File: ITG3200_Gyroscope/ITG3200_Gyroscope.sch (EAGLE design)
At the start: 11 parts, among them U1 ITG-3200

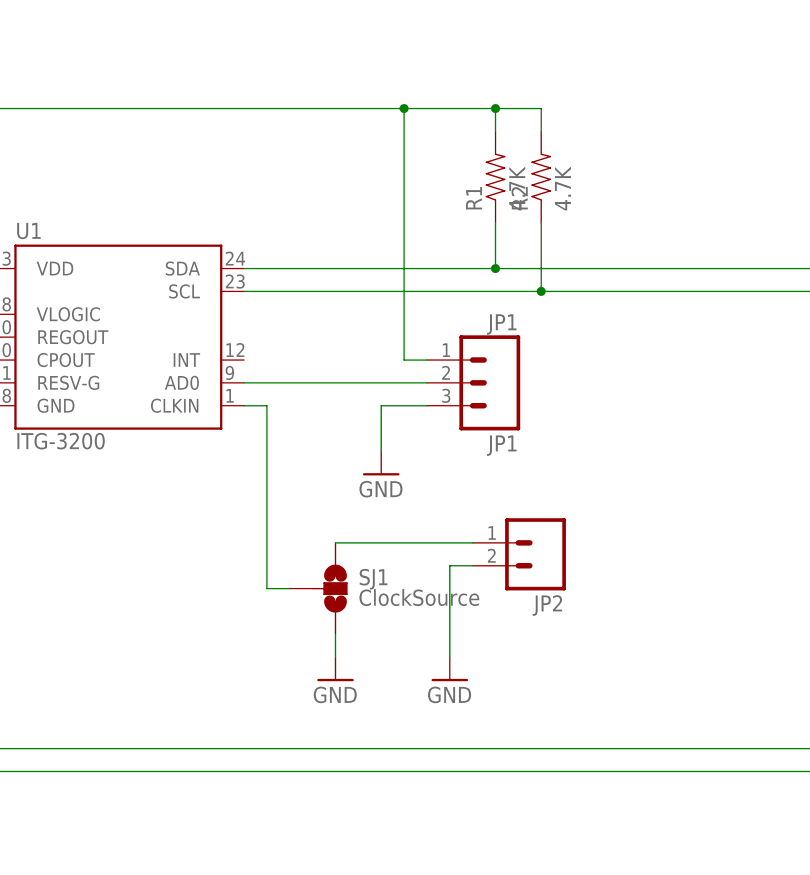
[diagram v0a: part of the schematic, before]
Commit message: Added OLED Shield Added LiPo Battery Charger Shield Updated outlines of all shields to match the cutout of the nodemcu board
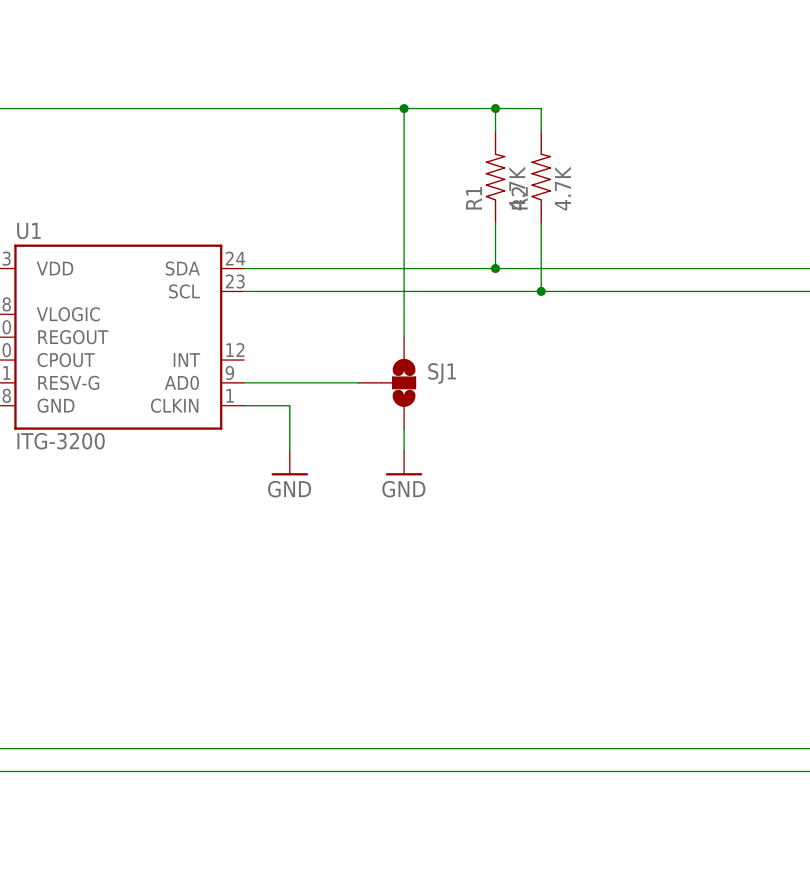
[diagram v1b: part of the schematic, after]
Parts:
- removed JP1: JP1, SparkFun:M03PTH
- removed JP2: (no value), SparkFun:M02LOCK
- SJ1: value ClockSource -> (none); device SparkFun:SOLDERJUMPER_2WAYPASTE2&3 -> SparkFun:SOLDERJUMPER_2WAYT
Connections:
- removed net N$10: JP2.1, SJ1.1
- removed net N$11: SJ1.2, U1.CLKIN
- net +3V3: now also SJ1.1; no longer JP1.1
- net GND: now also U1.CLKIN; no longer JP1.3, JP2.2
- net N$1: now also SJ1.2; no longer JP1.2
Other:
- moved on the sheet: SJ1
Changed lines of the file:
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@@
 <?xml version="1.0" encoding="utf-8"?>
 <!DOCTYPE eagle SYSTEM "eagle.dtd">
-<eagle version="7.3.0">
+<eagle version="7.4.0">
 <drawing>
 <settings>
@@
 <part name="R2" library="SparkFun" deviceset="RESISTOR" device="0402-RES" value="4.7K"/>
 <part name="+3V2" library="supply1" deviceset="+3V3" device=""/>
-<part name="JP1" library="SparkFun" deviceset="M03" device="PTH" value="JP1"/>
 <part name="GND7" library="SparkFun" deviceset="GND" device=""/>
 <part name="U1" library="SparkFun" deviceset="ITG-3200" device=""/>
@@
 <part name="GND10" library="SparkFun" deviceset="GND" device=""/>
 <part name="GND11" library="SparkFun" deviceset="GND" device=""/>
-<part name="JP2" library="SparkFun" deviceset="M02" device="LOCK"/>
 <part name="GND12" library="SparkFun" deviceset="GND" device=""/>
-<part name="SJ1" library="SparkFun" deviceset="SOLDERJUMPER_2WAY" device="PASTE2&amp;3" value="ClockSource"/>
-<part name="GND13" library="SparkFun" deviceset="GND" device=""/>
 <part name="U$2" library="NerduinoShieldLib" deviceset="NERDSHIELD" device=""/>
 <part name="+3V4" library="supply1" deviceset="+3V3" device=""/>
+<part name="SJ1" library="SparkFun" deviceset="SOLDERJUMPER_2WAY" device="T"/>
 </parts>
 <sheets>
@@
 <instance part="R2" gate="G$1" x="177.8" y="114.3" rot="R90"/>
 <instance part="+3V2" gate="G$1" x="96.52" y="129.54"/>
-<instance part="JP1" gate="G$1" x="172.72" y="91.44" rot="R180"/>
-<instance part="GND7" gate="1" x="160.02" y="81.28"/>
+<instance part="GND7" gate="1" x="162.56" y="81.28"/>
 <instance part="U1" gate="G$1" x="129.54" y="96.52"/>
 <instance part="GND8" gate="1" x="114.3" y="83.82"/>
@@
 <instance part="GND10" gate="1" x="93.98" y="78.74"/>
 <instance part="GND11" gate="1" x="86.36" y="78.74"/>
-<instance part="JP2" gate="G$1" x="177.8" y="73.66" rot="R180"/>
-<instance part="GND12" gate="1" x="154.94" y="58.42"/>
-<instance part="SJ1" gate="G$1" x="154.94" y="68.58"/>
-<instance part="GND13" gate="1" x="167.64" y="58.42"/>
+<instance part="GND12" gate="1" x="149.86" y="81.28"/>
 <instance part="U$2" gate="G$1" x="40.64" y="53.34"/>
 <instance part="+3V4" gate="G$1" x="93.98" y="43.18"/>
+<instance part="SJ1" gate="G$1" x="162.56" y="91.44"/>
 </instances>
 <busses>
@@
 </segment>
 <segment>
-<wire x1="165.1" y1="88.9" x2="160.02" y2="88.9" width="0.1524" layer="91"/>
-<wire x1="160.02" y1="88.9" x2="160.02" y2="83.82" width="0.1524" layer="91"/>
-<pinref part="JP1" gate="G$1" pin="3"/>
 <pinref part="GND7" gate="1" pin="GND"/>
+<pinref part="SJ1" gate="G$1" pin="3"/>
+<wire x1="162.56" y1="83.82" x2="162.56" y2="86.36" width="0.1524" layer="91"/>
 </segment>
 <segment>
@@
 </segment>
 <segment>
-<wire x1="154.94" y1="60.96" x2="154.94" y2="63.5" width="0.1524" layer="91"/>
-<pinref part="SJ1" gate="G$1" pin="3"/>
-<pinref part="GND12" gate="1" pin="GND"/>
-</segment>
-<segment>
-<wire x1="170.18" y1="71.12" x2="167.64" y2="71.12" width="0.1524" layer="91"/>
-<wire x1="167.64" y1="71.12" x2="167.64" y2="60.96" width="0.1524" layer="91"/>
-<pinref part="JP2" gate="G$1" pin="2"/>
-<pinref part="GND13" gate="1" pin="GND"/>
-</segment>
-<segment>
 <pinref part="U$2" gate="G$1" pin="GND$17"/>
 <pinref part="GND1" gate="1" pin="GND"/>
@@
 <wire x1="17.78" y1="48.26" x2="17.78" y2="38.1" width="0.1524" layer="91"/>
 <junction x="17.78" y="38.1"/>
+</segment>
+<segment>
+<pinref part="U1" gate="G$1" pin="CLKIN"/>
+<pinref part="GND12" gate="1" pin="GND"/>
+<wire x1="144.78" y1="88.9" x2="149.86" y2="88.9" width="0.1524" layer="91"/>
+<wire x1="149.86" y1="88.9" x2="149.86" y2="83.82" width="0.1524" layer="91"/>
 </segment>
 </net>
@@
 <wire x1="109.22" y1="121.92" x2="162.56" y2="121.92" width="0.1524" layer="91"/>
 <wire x1="162.56" y1="121.92" x2="172.72" y2="121.92" width="0.1524" layer="91"/>
-<wire x1="165.1" y1="93.98" x2="162.56" y2="93.98" width="0.1524" layer="91"/>
-<wire x1="162.56" y1="93.98" x2="162.56" y2="121.92" width="0.1524" layer="91"/>
+<wire x1="162.56" y1="96.52" x2="162.56" y2="121.92" width="0.1524" layer="91"/>
 <junction x="172.72" y="121.92"/>
 <junction x="96.52" y="121.92"/>
@@
 <pinref part="+3V2" gate="G$1" pin="+3V3"/>
 <pinref part="U1" gate="G$1" pin="VDD"/>
-<pinref part="JP1" gate="G$1" pin="1"/>
+<pinref part="SJ1" gate="G$1" pin="1"/>
 </segment>
 <segment>
@@
 <net name="N$1" class="0">
 <segment>
-<wire x1="165.1" y1="91.44" x2="144.78" y2="91.44" width="0.1524" layer="91"/>
-<pinref part="JP1" gate="G$1" pin="2"/>
+<wire x1="157.48" y1="91.44" x2="144.78" y2="91.44" width="0.1524" layer="91"/>
 <pinref part="U1" gate="G$1" pin="AD0"/>
+<pinref part="SJ1" gate="G$1" pin="2"/>
 </segment>
 </net>
@@
 </segment>
 </net>
-<net name="N$10" class="0">
-<segment>
-<wire x1="170.18" y1="73.66" x2="154.94" y2="73.66" width="0.1524" layer="91"/>
-<pinref part="SJ1" gate="G$1" pin="1"/>
-<pinref part="JP2" gate="G$1" pin="1"/>
-</segment>
-</net>
-<net name="N$11" class="0">
-<segment>
-<wire x1="149.86" y1="68.58" x2="147.32" y2="68.58" width="0.1524" layer="91"/>
-<wire x1="147.32" y1="68.58" x2="147.32" y2="88.9" width="0.1524" layer="91"/>
-<wire x1="147.32" y1="88.9" x2="144.78" y2="88.9" width="0.1524" layer="91"/>
-<pinref part="SJ1" gate="G$1" pin="2"/>
-<pinref part="U1" gate="G$1" pin="CLKIN"/>
-</segment>
-</net>

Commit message: Updated the i2c pins to all shields to use d11/d12  as these pins will have dual use with the upcoming wifimcu Added FM24W256  Fram shield Added X95840 Digital potentiometer Shield Added AD5696 DAC Shield
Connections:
- net GND: no longer U$2.GND$24
- net N$2: now also U$2.D11/GPIO09/SDD2; no longer U$2.D7/GPIO13/RXD2/HSPID/SDA
- net N$5: now also U$2.D12/GPIO10/SDD3; no longer U$2.D6/GPIO12/HSPIQ/SCL
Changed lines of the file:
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@@
 <wire x1="86.36" y1="38.1" x2="88.9" y2="38.1" width="0.1524" layer="91"/>
 <wire x1="88.9" y1="38.1" x2="88.9" y2="30.48" width="0.1524" layer="91"/>
-<pinref part="U$2" gate="G$1" pin="GND$24"/>
-<wire x1="86.36" y1="55.88" x2="88.9" y2="55.88" width="0.1524" layer="91"/>
-<wire x1="88.9" y1="55.88" x2="88.9" y2="38.1" width="0.1524" layer="91"/>
-<junction x="88.9" y="38.1"/>
 </segment>
 <segment>
@@
 <pinref part="R1" gate="G$1" pin="1"/>
 <pinref part="U1" gate="G$1" pin="SDA"/>
-<wire x1="223.52" y1="104.14" x2="223.52" y2="48.26" width="0.1524" layer="91"/>
-<wire x1="223.52" y1="48.26" x2="86.36" y2="48.26" width="0.1524" layer="91"/>
-<pinref part="U$2" gate="G$1" pin="D7/GPIO13/RXD2/HSPID/SDA"/>
-<wire x1="172.72" y1="104.14" x2="223.52" y2="104.14" width="0.1524" layer="91"/>
+<wire x1="172.72" y1="104.14" x2="208.28" y2="104.14" width="0.1524" layer="91"/>
+<pinref part="U$2" gate="G$1" pin="D11/GPIO09/SDD2"/>
+<wire x1="22.86" y1="60.96" x2="12.7" y2="60.96" width="0.1524" layer="91"/>
+<wire x1="12.7" y1="60.96" x2="12.7" y2="147.32" width="0.1524" layer="91"/>
+<wire x1="12.7" y1="147.32" x2="208.28" y2="147.32" width="0.1524" layer="91"/>
+<wire x1="208.28" y1="147.32" x2="208.28" y2="104.14" width="0.1524" layer="91"/>
 </segment>
 </net>
@@
 <pinref part="R2" gate="G$1" pin="1"/>
 <pinref part="U1" gate="G$1" pin="SCL"/>
-<wire x1="86.36" y1="50.8" x2="220.98" y2="50.8" width="0.1524" layer="91"/>
-<wire x1="220.98" y1="50.8" x2="220.98" y2="101.6" width="0.1524" layer="91"/>
-<pinref part="U$2" gate="G$1" pin="D6/GPIO12/HSPIQ/SCL"/>
-<wire x1="177.8" y1="101.6" x2="220.98" y2="101.6" width="0.1524" layer="91"/>
+<wire x1="177.8" y1="101.6" x2="203.2" y2="101.6" width="0.1524" layer="91"/>
+<wire x1="203.2" y1="101.6" x2="203.2" y2="144.78" width="0.1524" layer="91"/>
+<wire x1="203.2" y1="144.78" x2="15.24" y2="144.78" width="0.1524" layer="91"/>
+<wire x1="15.24" y1="144.78" x2="15.24" y2="63.5" width="0.1524" layer="91"/>
+<pinref part="U$2" gate="G$1" pin="D12/GPIO10/SDD3"/>
+<wire x1="15.24" y1="63.5" x2="22.86" y2="63.5" width="0.1524" layer="91"/>
 </segment>
 </net>
